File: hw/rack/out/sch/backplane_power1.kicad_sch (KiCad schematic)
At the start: 42 parts, among them J1 12V IN, J5 CM4IO 12V, Q1 AO4407A, U1 TPS259541DSGR, U12 TPS259541DSGR, U2 TPS62933DRLR, U3 TLV76733

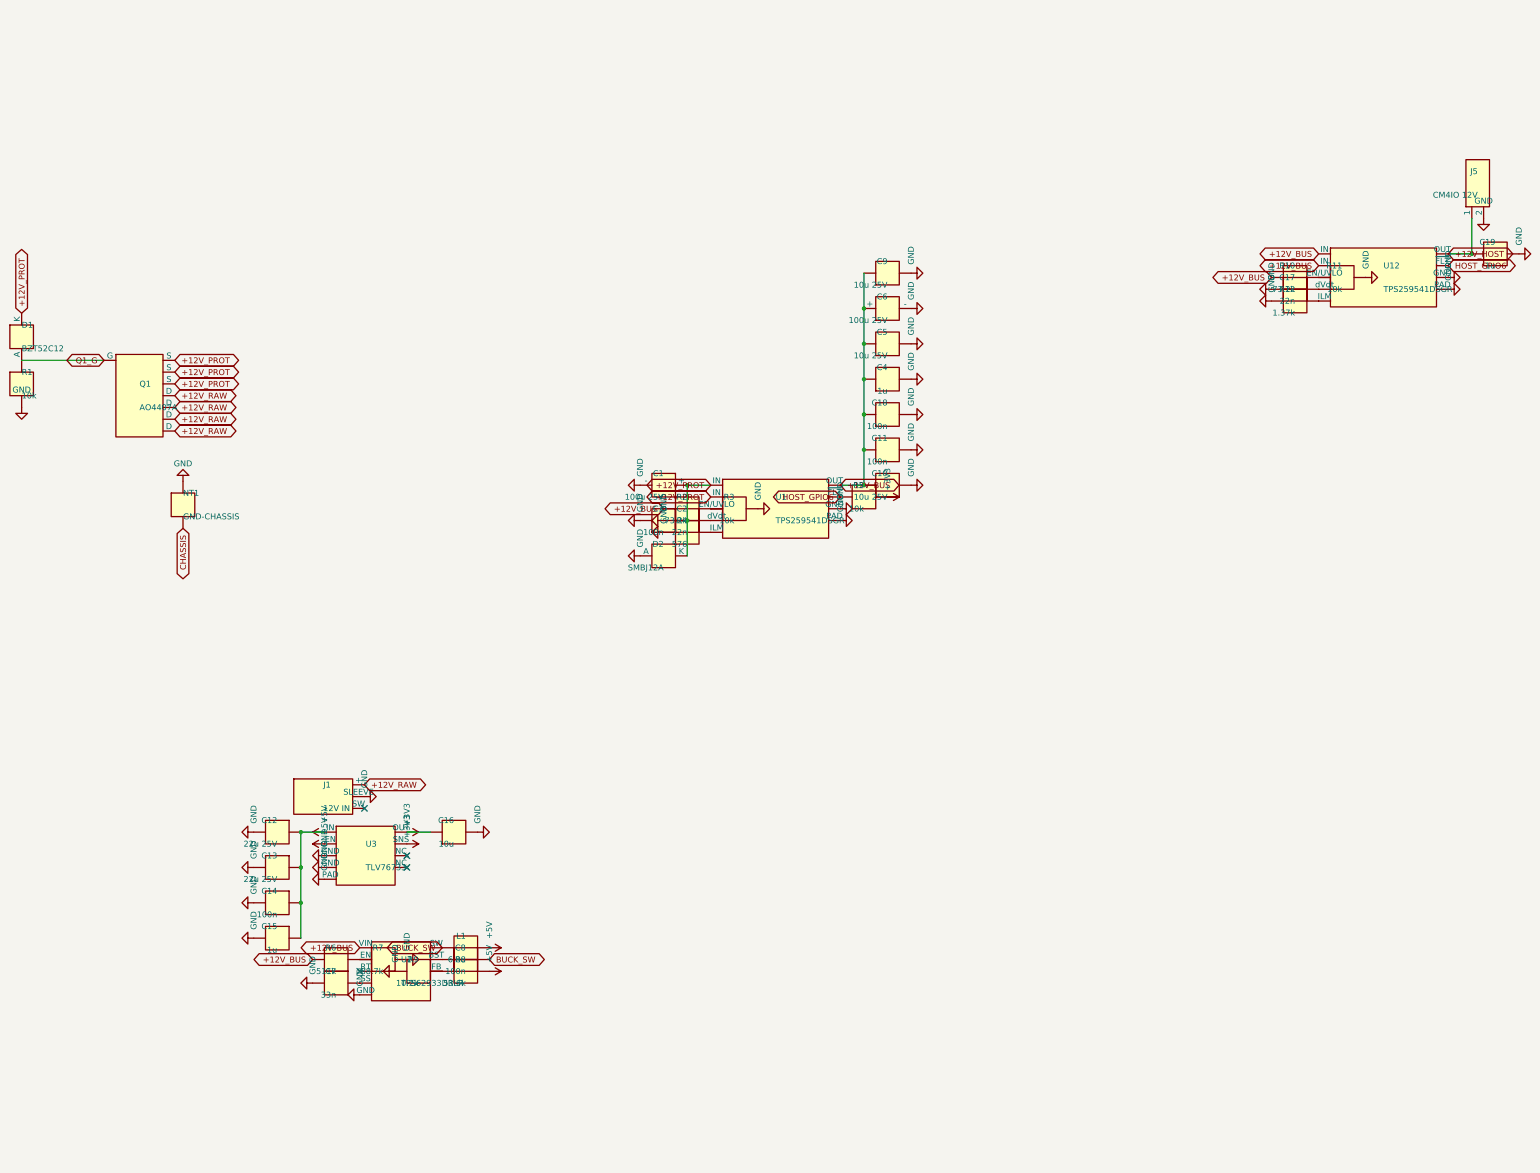
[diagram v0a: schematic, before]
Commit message: hw/rack: #95 review fixes: QPQ1907 pinout + RF continuity test, 1 ohm 2512 bias-T, input fuse, keyed slots, CM4 source, CI scikit-rf + stale check, ADR-0018 gain-plan stop-and-ask (#33)
- QPQ1907 pins per datasheet 040820 (1 in, 4 out, 2/3/5 GND); test walks BNC to every slot port
- bias-T 1 ohm 2512 (0.27 W at 0.52 A), resistor power ratings asserted
- 4 A fuse ahead of the TVS; Harwin M20-7831346 + M20-003 key at position 14
- CM4002008 from The Pi Hut (GBP 79.20); Lite-On LEDs
- Wilkinson +-10 % width sweep; netlist timestamp stripped
- CI: scikit-rf installed, cross-check required under CI, hw/rack stale-output diff
- Audit 6: per-carrier NF, stage headroom at 0.5/1/1.5 m (wings), phones, nRF5340 PS v1.1
  C/I + PIMD, nRF21540 P1dB; no fixed gain plan meets both: stop-and-ask

Co-Authored-By: Claude Opus 5.5 <noreply@anthropic.com>
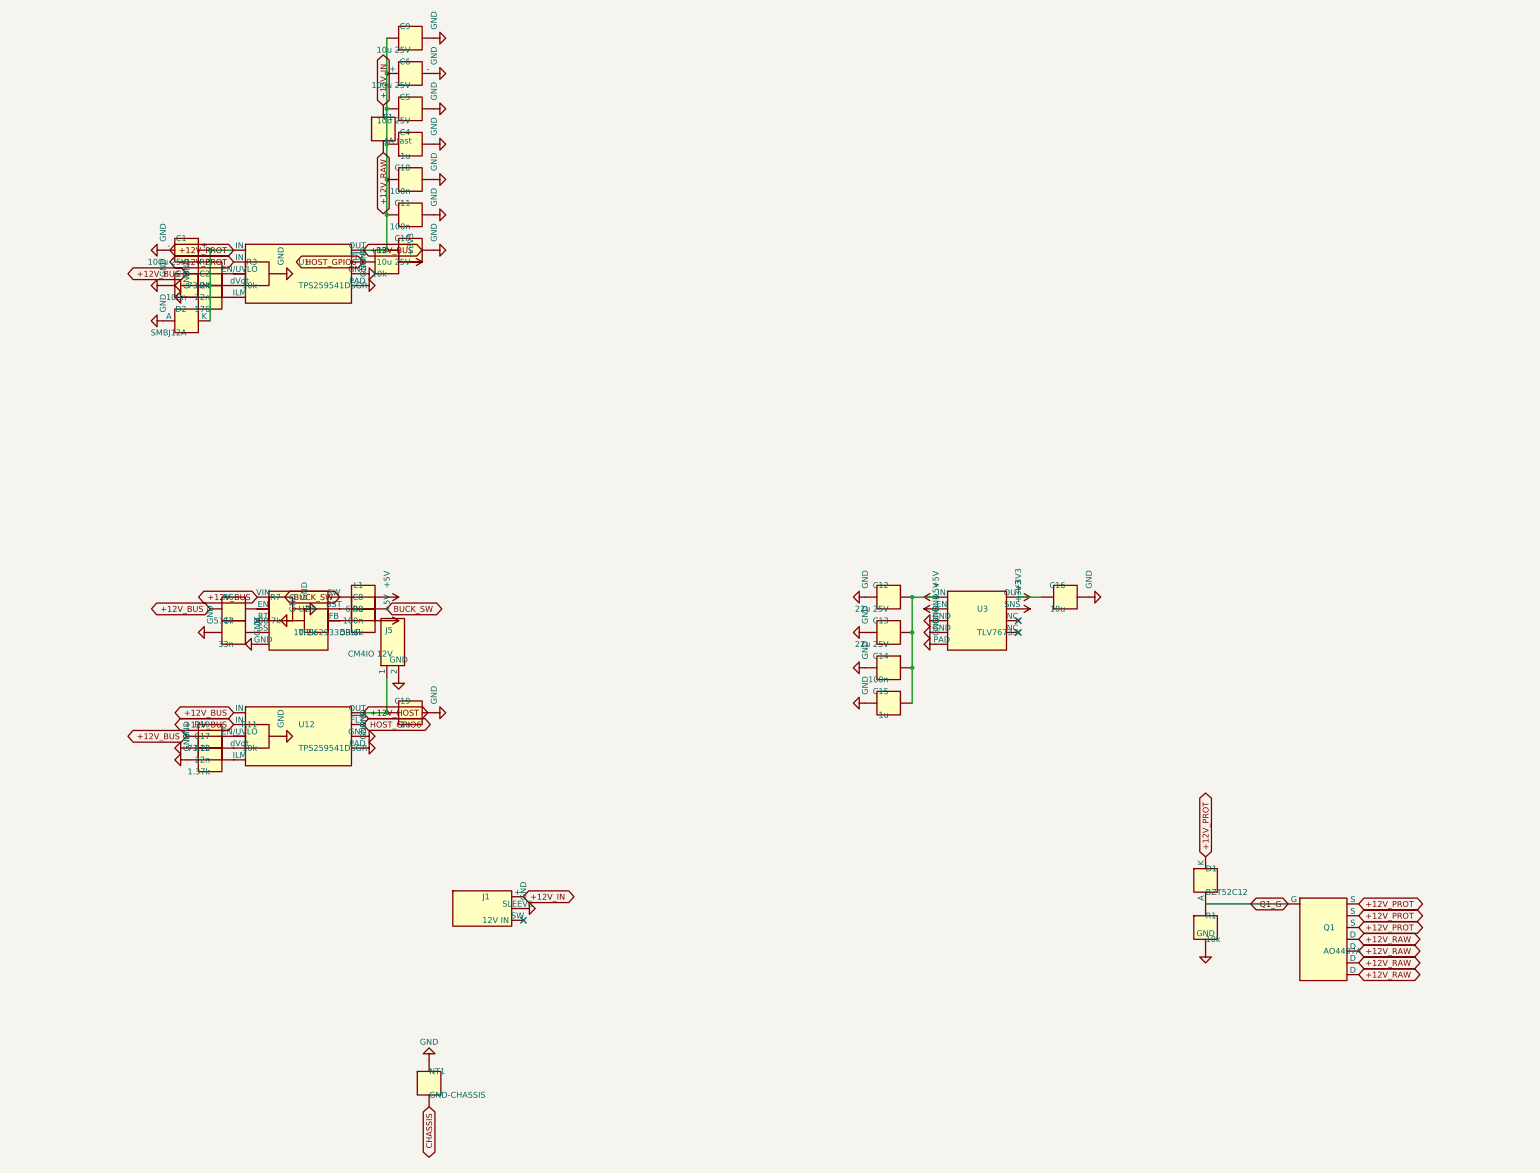
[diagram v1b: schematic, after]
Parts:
- added F1: 4A fast, Fuse:Fuse_Littelfuse_NANO2_451_453, symbol openpack_rack:Fuse
- R1, R10, R11, R12, R2, R3, R4, R5, R6, R7, R8, R9: P_W (none) -> 0.0625
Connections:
- net +12V_RAW: now also F1.2; no longer J1.1 (+)
- new net +12V_IN: F1.1, J1.1 (+)
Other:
- moved on the sheet: C1, C10, C11, C12, C13, C14, C15, C16, C17, C18, C19, C2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
